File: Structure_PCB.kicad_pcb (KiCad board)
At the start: 2 copper layers, 180 x 100 mm, 25 parts, among them J10 JST-GH 4Pin, J11 JST-GH 4Pin, J12 JST-GH 4Pin, J6 6620XX236022_662004236022, J9 Conn_02x04_Top_Bottom, K2 FINDER-30.22

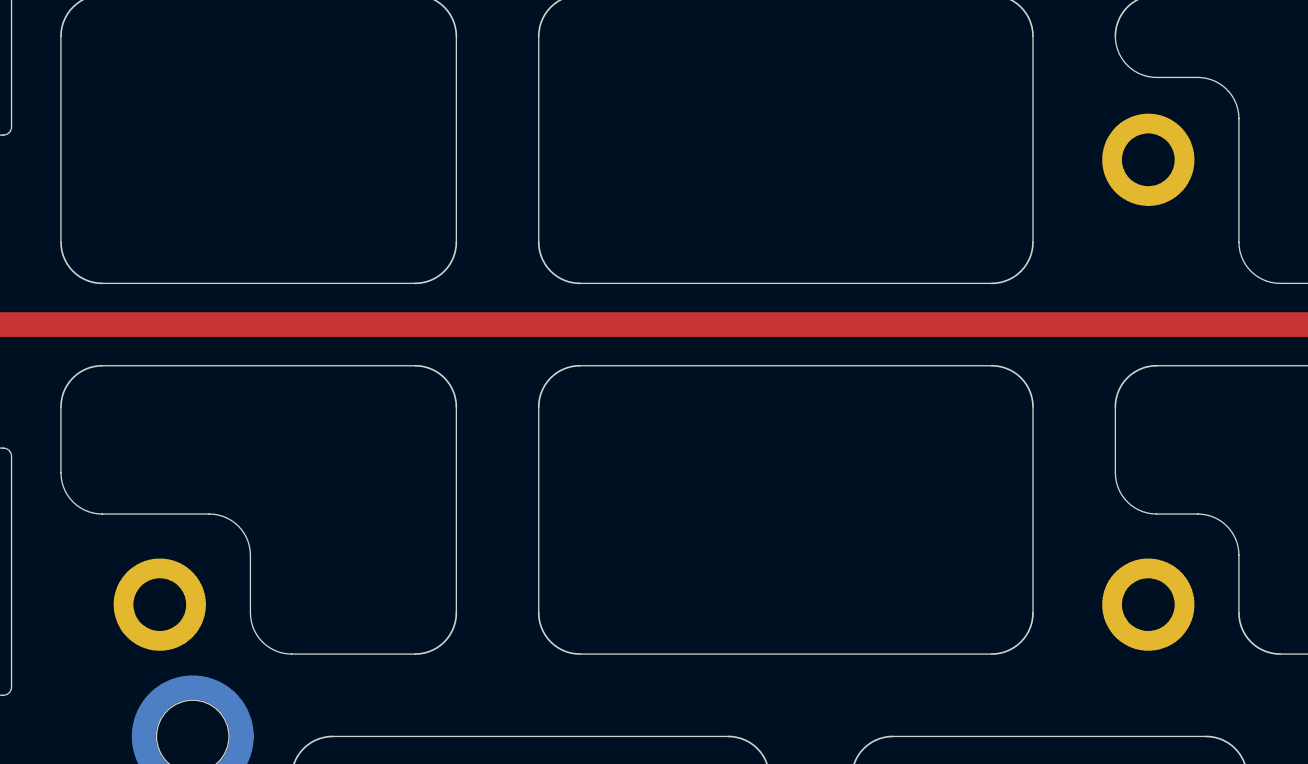
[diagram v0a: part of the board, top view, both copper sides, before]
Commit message: added correct footprint vor vega mount
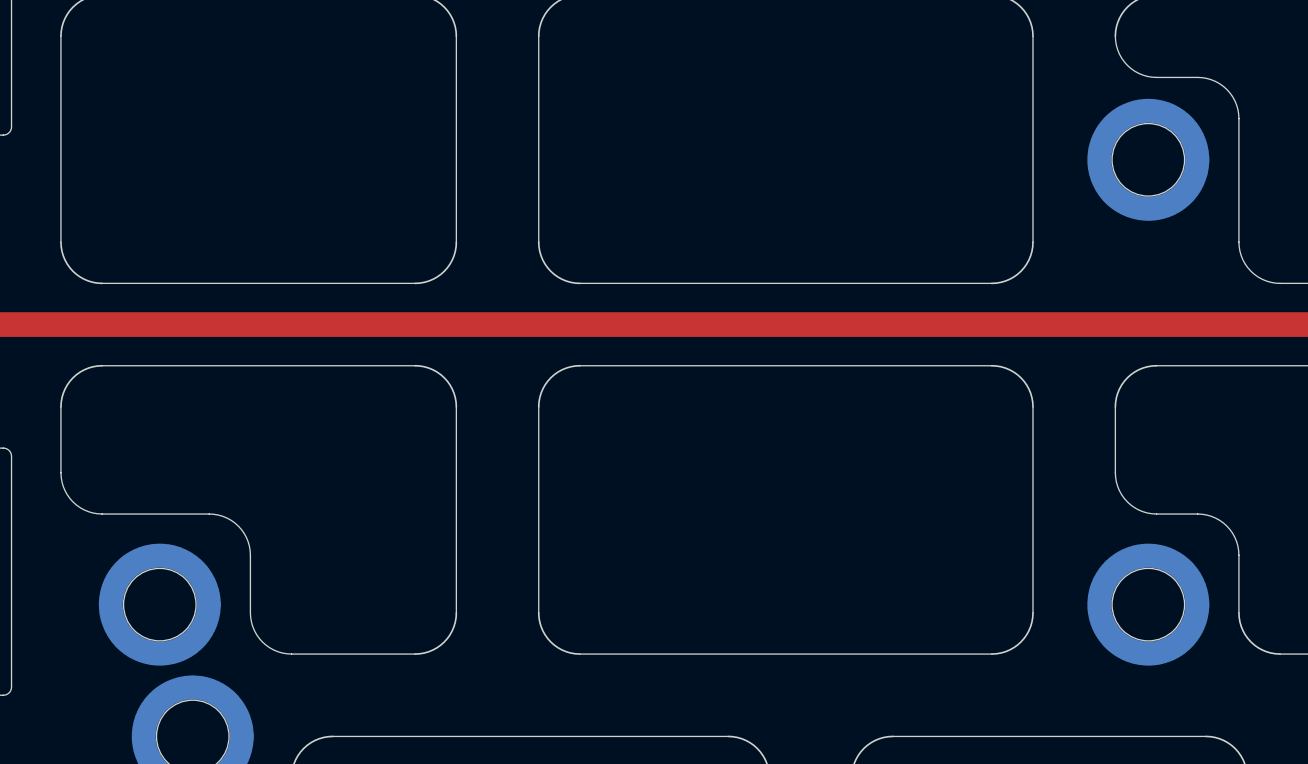
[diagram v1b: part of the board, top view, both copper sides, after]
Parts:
- H13, H14, H15: footprint MountingHole:MountingHole_3.2mm_M3_DIN965_Pad -> Mounting_Wuerth:Mounting_Wuerth_WA-SMSR-3.2mm_H4.6mm_ReverseMount_9775046960; moved to B.Cu

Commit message: small correction of vega layout
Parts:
- moved H13 27.0 mm to (108.0, 90.0)
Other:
- outline, holes or cut-outs redrawn
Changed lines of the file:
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@@
 	(footprint "Mounting_Wuerth:Mounting_Wuerth_WA-SMSR-3.2mm_H4.6mm_ReverseMount_9775046960"
 		(layer "B.Cu")
-		(at 108 117)
+		(at 108 90)
 		(descr "Mounting Hardware, inside through hole 3.2mm, height 4.6, Wuerth electronics 9775046960 (https://katalog.we-online.com/em/datasheet/9775046960.pdf), generated with kicad-footprint-generator")
 		(tags "Mounting 3.2mm 9775046960")
@@
 		(layer "Edge.Cuts")
 	)
+	(gr_arc
+		(start 103.5 84)
+		(mid 102.43934 83.56066)
+		(end 102 82.5)
+		(stroke
+			(width 0.05)
+			(type default)
+		)
+		(layer "Edge.Cuts")
+	)
 	(gr_line
 		(start 76 88)
@@
 	)
 	(gr_line
-		(start 113.5 117.5)
-		(end 113.5 114)
+		(start 103.5 84)
+		(end 111.5 84)
 		(stroke
 			(width 0.05)
@@
 	)
 	(gr_arc
-		(start 102 82.5)
-		(mid 102.732233 80.732233)
-		(end 104.5 80)
+		(start 102 81.5)
+		(mid 102.43934 80.43934)
+		(end 103.5 80)
 		(stroke
 			(width 0.1)
@@
 	(gr_line
 		(start 123.5 80)
-		(end 104.5 80)
+		(end 103.5 80)
 		(stroke
 			(width 0.05)
@@
 	)
 	(gr_line
-		(start 104.5 97.5)
+		(start 116.5 97.5)
 		(end 123.5 97.5)
 		(stroke
@@
 	)
 	(gr_arc
-		(start 104.5 97.5)
-		(mid 102.732233 96.767767)
-		(end 102 95)
+		(start 116.5 97.5)
+		(mid 114.732233 96.767767)
+		(end 114 95)
 		(stroke
 			(width 0.1)
@@
 	)
 	(gr_arc
-		(start 111 111.5)
-		(mid 112.767767 112.232233)
-		(end 113.5 114)
+		(start 111.5 84)
+		(mid 113.267767 84.732233)
+		(end 114 86.5)
 		(stroke
 			(width 0.05)
@@
 	)
 	(gr_arc
-		(start 116 120)
-		(mid 114.232233 119.267767)
-		(end 113.5 117.5)
+		(start 104.5 120)
+		(mid 102.732233 119.267767)
+		(end 102 117.5)
 		(stroke
 			(width 0.05)
@@
 	(gr_line
 		(start 123.5 120)
-		(end 116 120)
+		(end 104.5 120)
 		(stroke
 			(width 0.05)
@@
 		(start 152.5 60)
 		(end 171.5 60)
-		(stroke
-			(width 0.05)
-			(type default)
-		)
-		(layer "Edge.Cuts")
-	)
-	(gr_line
-		(start 102 95)
-		(end 102 82.5)
 		(stroke
 			(width 0.05)
@@
 	)
 	(gr_arc
-		(start 104.5 111.5)
-		(mid 102.732233 110.767767)
-		(end 102 109)
-		(stroke
-			(width 0.05)
-			(type default)
-		)
-		(layer "Edge.Cuts")
-	)
-	(gr_arc
 		(start 134 147.25)
 		(mid 134.146447 146.896447)
@@
 	)
 	(gr_line
+		(start 102 82.5)
+		(end 102 81.5)
+		(stroke
+			(width 0.05)
+			(type default)
+		)
+		(layer "Edge.Cuts")
+	)
+	(gr_line
 		(start 73.3 130.75)
 		(end 73.3 122.25)
@@
 	)
 	(gr_line
-		(start 102 109)
+		(start 102 117.5)
 		(end 102 105)
 		(stroke
@@
 	)
 	(gr_line
-		(start 104.5 111.5)
-		(end 111 111.5)
-		(stroke
-			(width 0.05)
+		(start 114 95)
+		(end 114 86.5)
+		(stroke
+			(width 0.05)

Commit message: some layout changes
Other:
- outline, holes or cut-outs redrawn
- board text added: "pw.+"
- board text removed: "pw. good"

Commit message: most recent changes to layout, changed some components for hand soldering
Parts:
- D4, D5, D6: footprint Diode_SMD:D_SOD-323 -> Diode_SMD:D_SOD-123F
- F1: footprint Fuse:Fuse_0603_1608Metric_Pad1.05x0.95mm_HandSolder -> Fuse:Fuse_1206_3216Metric_Pad1.42x1.75mm_HandSolder
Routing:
- net /SBout: track 218.9 -> 217.2 mm
- net /pre_fuse: track 38.2 -> 37.4 mm

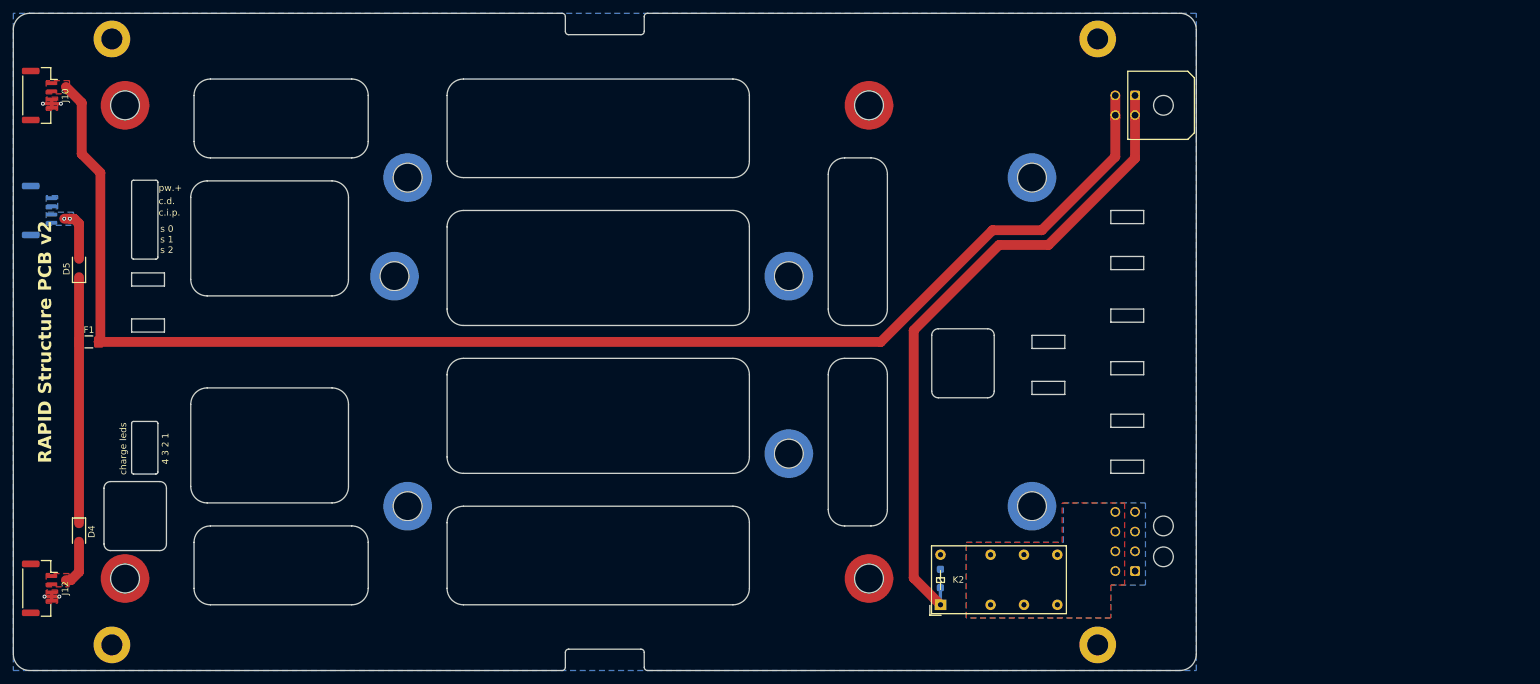
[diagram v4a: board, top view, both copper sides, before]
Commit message: changes to layout, added EB
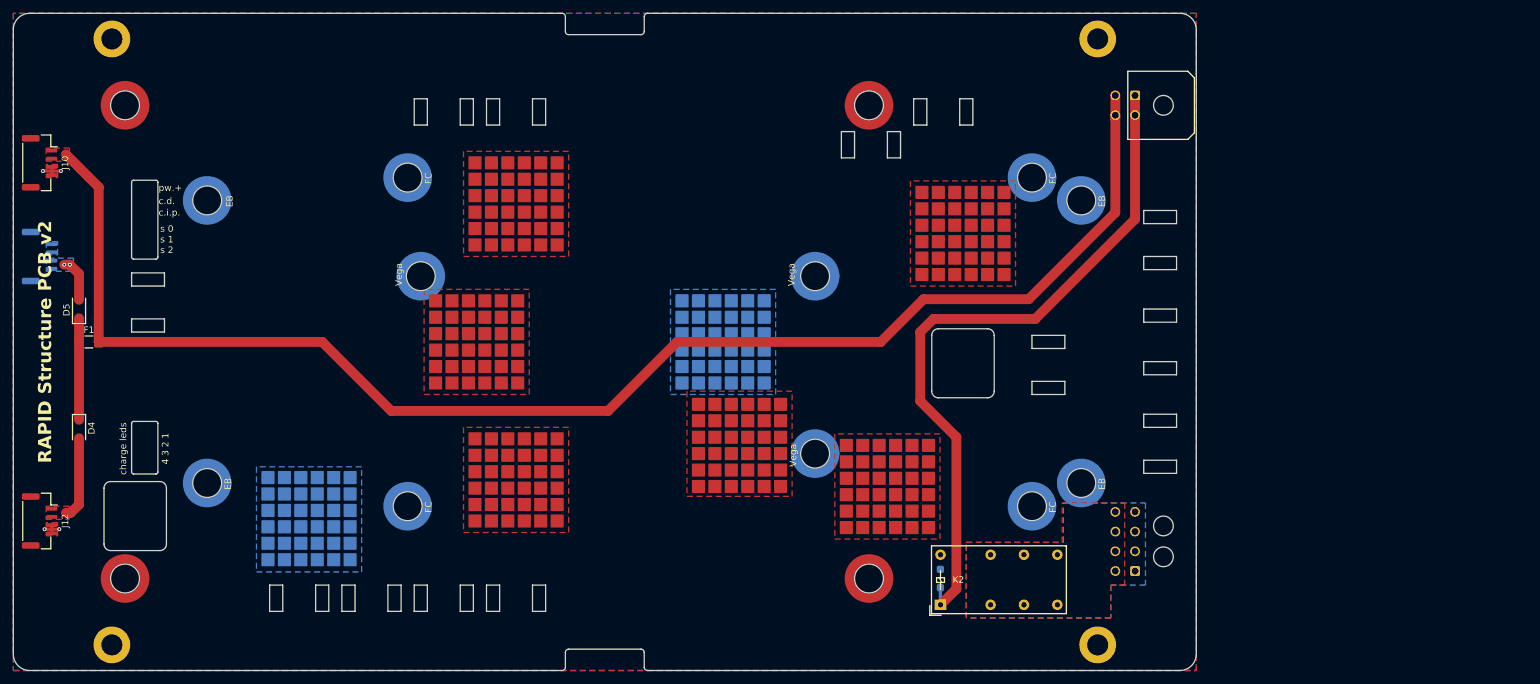
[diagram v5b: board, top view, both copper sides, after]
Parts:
- added H16: MountingHole, Mounting_Wuerth:Mounting_Wuerth_WA-SMSR-3.2mm_H4.6mm_ReverseMount_9775046960, B.Cu at (79.5, 121.5)
- added H17: MountingHole, Mounting_Wuerth:Mounting_Wuerth_WA-SMSR-3.2mm_H4.6mm_ReverseMount_9775046960, B.Cu at (79.5, 78.5)
- added H18: MountingHole, Mounting_Wuerth:Mounting_Wuerth_WA-SMSR-3.2mm_H4.6mm_ReverseMount_9775046960, B.Cu at (212.5, 121.5)
- added H19: MountingHole, Mounting_Wuerth:Mounting_Wuerth_WA-SMSR-3.2mm_H4.6mm_ReverseMount_9775046960, B.Cu at (212.5, 78.5)
- added HS10: Heatsink_Pad, Heatsink:würth 5x5 heat pads, F.Cu at (155.5, 115.8)
- added HS11: Heatsink_Pad, Heatsink:würth 5x5 heat pads, F.Cu at (155.5, 120.8)
- added HS12: Heatsink_Pad, Heatsink:würth 5x5 heat pads, F.Cu at (160.5, 110.8)
- added HS13: Heatsink_Pad, Heatsink:würth 5x5 heat pads, F.Cu at (160.5, 115.8)
- added HS14: Heatsink_Pad, Heatsink:würth 5x5 heat pads, F.Cu at (160.5, 120.8)
- added HS15: Heatsink_Pad, Heatsink:würth 5x5 heat pads, F.Cu at (165.5, 110.8)
- added HS16: Heatsink_Pad, Heatsink:würth 5x5 heat pads, F.Cu at (178.0, 117.0)
- added HS17: Heatsink_Pad, Heatsink:würth 5x5 heat pads, F.Cu at (178.0, 122.0)
- added HS18: Heatsink_Pad, Heatsink:würth 5x5 heat pads, F.Cu at (178.0, 127.0)
- added HS19: Heatsink_Pad, Heatsink:würth 5x5 heat pads, F.Cu at (183.0, 127.0)
- added HS20: Heatsink_Pad, Heatsink:würth 5x5 heat pads, F.Cu at (183.0, 122.0)
- added HS21: Heatsink_Pad, Heatsink:würth 5x5 heat pads, F.Cu at (183.0, 117.0)
- added HS22: Heatsink_Pad, Heatsink:würth 5x5 heat pads, F.Cu at (121.5, 116.0)
- added HS23: Heatsink_Pad, Heatsink:würth 5x5 heat pads, F.Cu at (189.5, 83.5)
- added HS24: Heatsink_Pad, Heatsink:würth 5x5 heat pads, F.Cu at (126.5, 116.0)
- added HS25: Heatsink_Pad, Heatsink:würth 5x5 heat pads, F.Cu at (189.5, 78.5)
- added HS26: Heatsink_Pad, Heatsink:würth 5x5 heat pads, F.Cu at (194.5, 78.5)
- added HS27: Heatsink_Pad, Heatsink:würth 5x5 heat pads, F.Cu at (199.5, 78.5)
- added HS28: Heatsink_Pad, Heatsink:würth 5x5 heat pads, F.Cu at (194.5, 88.5)
- added HS29: Heatsink_Pad, Heatsink:würth 5x5 heat pads, F.Cu at (199.5, 83.5)
- added HS30: Heatsink_Pad, Heatsink:würth 5x5 heat pads, F.Cu at (189.5, 88.5)
- added HS31: Heatsink_Pad, Heatsink:würth 5x5 heat pads, F.Cu at (194.5, 83.5)
- added HS32: Heatsink_Pad, Heatsink:würth 5x5 heat pads, F.Cu at (199.5, 88.5)
- added HS33: Heatsink_Pad, Heatsink:würth 5x5 heat pads, F.Cu at (165.5, 115.8)
- added HS34: Heatsink_Pad, Heatsink:würth 5x5 heat pads, F.Cu at (188.0, 117.0)
- added HS35: Heatsink_Pad, Heatsink:würth 5x5 heat pads, F.Cu at (188.0, 122.0)
- added HS36: Heatsink_Pad, Heatsink:würth 5x5 heat pads, F.Cu at (188.0, 127.0)
- added HS37: Heatsink_Pad, Heatsink:würth 5x5 heat pads, F.Cu at (165.5, 120.8)
- added HS42: Heatsink_Pad, Heatsink:würth 5x5 heat pads, F.Cu at (131.5, 116.0)
- added HS43: Heatsink_Pad, Heatsink:würth 5x5 heat pads, F.Cu at (126.5, 126.0)
- added HS44: Heatsink_Pad, Heatsink:würth 5x5 heat pads, F.Cu at (131.5, 121.0)
- added HS45: Heatsink_Pad, Heatsink:würth 5x5 heat pads, F.Cu at (131.5, 126.0)
- added HS46: Heatsink_Pad, Heatsink:würth 5x5 heat pads, F.Cu at (126.5, 121.0)
- added HS47: Heatsink_Pad, Heatsink:würth 5x5 heat pads, F.Cu at (121.5, 121.0)
- added HS48: Heatsink_Pad, Heatsink:würth 5x5 heat pads, F.Cu at (121.5, 126.0)
- added HS49: Heatsink_Pad, Heatsink:würth 5x5 heat pads, F.Cu at (121.5, 74.0)
- added HS50: Heatsink_Pad, Heatsink:würth 5x5 heat pads, F.Cu at (121.5, 79.0)
- added HS51: Heatsink_Pad, Heatsink:würth 5x5 heat pads, F.Cu at (121.5, 84.0)
- added HS52: Heatsink_Pad, Heatsink:würth 5x5 heat pads, F.Cu at (131.5, 79.0)
- added HS53: Heatsink_Pad, Heatsink:würth 5x5 heat pads, F.Cu at (131.5, 84.0)
- added HS54: Heatsink_Pad, Heatsink:würth 5x5 heat pads, F.Cu at (131.5, 74.0)
- added HS55: Heatsink_Pad, Heatsink:würth 5x5 heat pads, F.Cu at (126.5, 74.0)
- added HS56: Heatsink_Pad, Heatsink:würth 5x5 heat pads, F.Cu at (126.5, 79.0)
- added HS57: Heatsink_Pad, Heatsink:würth 5x5 heat pads, F.Cu at (126.5, 84.0)
- added HS58: Heatsink_Pad, Heatsink:würth 5x5 heat pads, F.Cu at (115.5, 95.0)
- added HS59: Heatsink_Pad, Heatsink:würth 5x5 heat pads, F.Cu at (125.5, 100.0)
- added HS60: Heatsink_Pad, Heatsink:würth 5x5 heat pads, F.Cu at (115.5, 105.0)
- added HS61: Heatsink_Pad, Heatsink:würth 5x5 heat pads, F.Cu at (120.5, 95.0)
- added HS62: Heatsink_Pad, Heatsink:würth 5x5 heat pads, F.Cu at (120.5, 100.0)
- added HS63: Heatsink_Pad, Heatsink:würth 5x5 heat pads, F.Cu at (120.5, 105.0)
- added HS64: Heatsink_Pad, Heatsink:würth 5x5 heat pads, F.Cu at (125.5, 95.0)
- added HS65: Heatsink_Pad, Heatsink:würth 5x5 heat pads, F.Cu at (115.5, 100.0)
- added HS66: Heatsink_Pad, Heatsink:würth 5x5 heat pads, F.Cu at (125.5, 105.0)
- added HS67: Heatsink_Pad, Heatsink:würth 5x5 heat pads, B.Cu at (95.0, 131.9)
- added HS68: Heatsink_Pad, Heatsink:würth 5x5 heat pads, B.Cu at (95.0, 126.9)
- added HS69: Heatsink_Pad, Heatsink:würth 5x5 heat pads, B.Cu at (95.0, 121.9)
- added HS70: Heatsink_Pad, Heatsink:würth 5x5 heat pads, B.Cu at (90.0, 131.9)
- added HS71: Heatsink_Pad, Heatsink:würth 5x5 heat pads, B.Cu at (90.0, 126.9)
- added HS72: Heatsink_Pad, Heatsink:würth 5x5 heat pads, B.Cu at (90.0, 121.9)
- added HS73: Heatsink_Pad, Heatsink:würth 5x5 heat pads, B.Cu at (100.0, 131.9)
- added HS74: Heatsink_Pad, Heatsink:würth 5x5 heat pads, B.Cu at (100.0, 126.9)
- added HS75: Heatsink_Pad, Heatsink:würth 5x5 heat pads, B.Cu at (100.0, 121.9)
- added HS76: Heatsink_Pad, Heatsink:würth 5x5 heat pads, B.Cu at (158.0, 105.0)
- added HS77: Heatsink_Pad, Heatsink:würth 5x5 heat pads, B.Cu at (158.0, 100.0)
- added HS78: Heatsink_Pad, Heatsink:würth 5x5 heat pads, B.Cu at (158.0, 95.0)
- added HS79: Heatsink_Pad, Heatsink:würth 5x5 heat pads, B.Cu at (153.0, 105.0)
- added HS80: Heatsink_Pad, Heatsink:würth 5x5 heat pads, B.Cu at (153.0, 100.0)
- added HS81: Heatsink_Pad, Heatsink:würth 5x5 heat pads, B.Cu at (153.0, 95.0)
- added HS82: Heatsink_Pad, Heatsink:würth 5x5 heat pads, B.Cu at (163.0, 105.0)
- added HS83: Heatsink_Pad, Heatsink:würth 5x5 heat pads, B.Cu at (163.0, 100.0)
- added HS84: Heatsink_Pad, Heatsink:würth 5x5 heat pads, B.Cu at (163.0, 95.0)
- added HS9: Heatsink_Pad, Heatsink:würth 5x5 heat pads, F.Cu at (155.5, 110.8)
- moved D4 15.8 mm to (60.0, 113.2)
- moved J10 10.2 mm to (54.0, 72.8)
- moved J12 10.2 mm to (54.0, 127.2)
- moved J11 7.00 mm to (54.0, 87.0)
- moved D5 6.25 mm to (60.0, 95.0)
- moved H13 4.00 mm to (112.0, 90.0)
- moved H14 4.00 mm to (172.0, 90.0)
- moved H15 4.00 mm to (172.0, 117.0)
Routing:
- net /pre_fuse: track 37.4 -> 15.4 mm
- net /post_arm: track 100.6 -> 106.5 mm
- net /SBin: track 7.12 -> 12.6 mm
- net /SBout: track 217.2 -> 220.5 mm
- net /PBin: track 7.91 -> 6.78 mm
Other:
- outline, holes or cut-outs redrawn
- board text added: "EB"
- board text added: "FC"
- board text added: "Vega"
